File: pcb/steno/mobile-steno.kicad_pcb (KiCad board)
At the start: 2 copper layers, 188 x 92.5 mm, 65 parts, among them J1 Conn_01x02, J2 Conn_01x04, J3 Conn_01x02, K1 KEYSW, K10 KEYSW, K11 KEYSW, K12 KEYSW, K13 KEYSW, K14 KEYSW, K15 KEYSW, K16 KEYSW, K17 KEYSW, K18 KEYSW, K19 KEYSW, K2 KEYSW, K20 KEYSW, K21 KEYSW, K22 KEYSW, K23 KEYSW, K24 KEYSW, K25 KEYSW, K26 KEYSW, K27 KEYSW, K28 KEYSW, K29 KEYSW, K3 KEYSW, K30 KEYSW, K4 KEYSW, K5 KEYSW, K6 KEYSW, K7 KEYSW, K8 KEYSW, K9 KEYSW, U1 Adafruit_Feather, U2 MT25QL128ABA1ESE

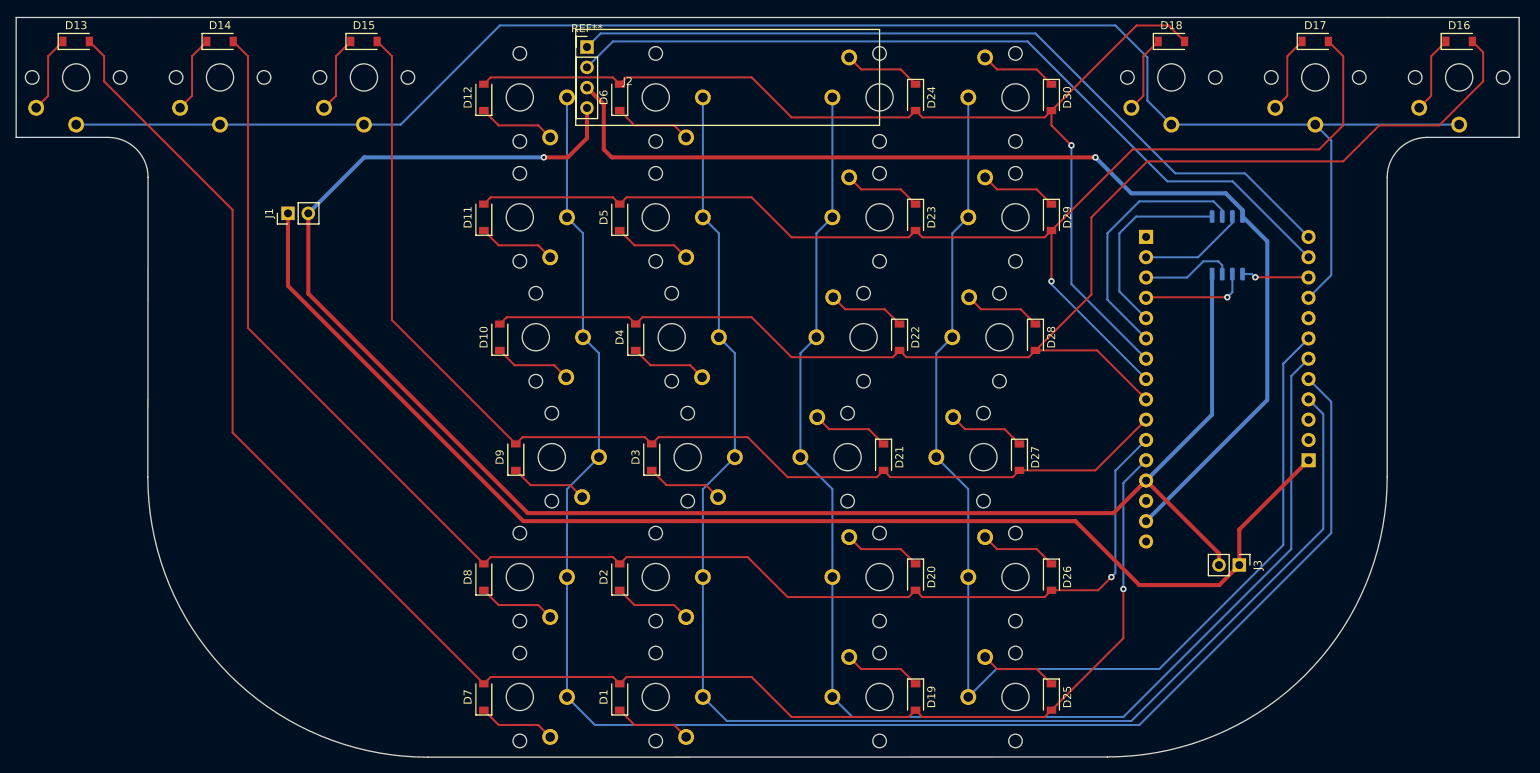
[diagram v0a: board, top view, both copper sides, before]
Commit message: Fix silkscreen and fucking flip the switches
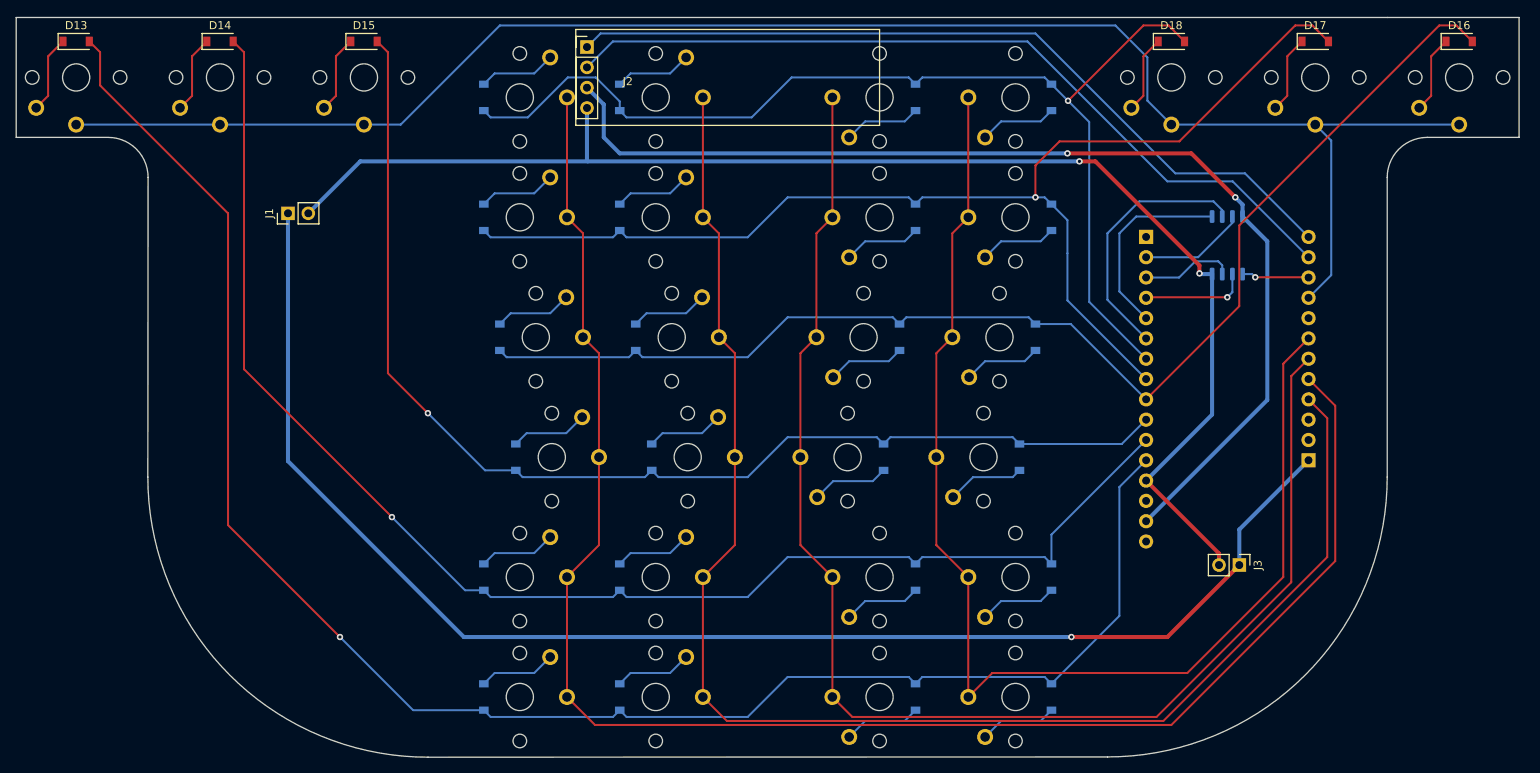
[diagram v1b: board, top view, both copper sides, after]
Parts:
- D1, D10, D11, D12, D19, D2, D20, D21, D22, D23, D24, D25, D26, D27, D28, D29, D3, D30, D4, D5, D6, D7, D8, D9, K1, K10, K11, K12, K19, K2, K20, K21, K22, K23, K24, K25, K26, K27, K28, K29, K3, K30, K4, K5, K6, K7, K8, K9: moved to B.Cu
- turned D1 to 270 degrees
- turned D10 to 270 degrees
- turned D11 to 270 degrees
- turned D12 to 270 degrees
- turned D19 to 90 degrees
- turned D2 to 270 degrees
- turned D20 to 90 degrees
- turned D21 to 90 degrees
- turned D22 to 90 degrees
- turned D23 to 90 degrees
- turned D24 to 90 degrees
- turned D25 to 90 degrees
- turned D26 to 90 degrees
- turned D27 to 90 degrees
- turned D28 to 90 degrees
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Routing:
- net GND: track 214.1 -> 172.6 mm, vias 1 -> 2
- net BAT: track 161.3 -> 179.5 mm, vias 0 -> 1
- net COL4: track 168.7 -> 155.9 mm
- net COL1: track 212.1 -> 217.3 mm
- net COL6: track 133.0 -> 137.8 mm
- net COL3: track 143.2 -> 147.4 mm, vias 0 -> 1
- net ROW2: track 205.8 -> 208.5 mm
- net ROW1: track 184.1 -> 186.8 mm
- net ROW4: track 170.2 -> 172.6 mm
- net ROW5: track 152.7 -> 155.1 mm
- net COL2: track 180.7 -> 178.6 mm
- net COL5: track 151.9 -> 150.7 mm
- net VCC: track 138.1 -> 137.6 mm, vias 1 -> 2
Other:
- board text added: "JLCJLCJLCJLC"

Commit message: Slightly improved layout and routing
- Moved thumb cluster to row 5 from 3
- Make row pins be in order
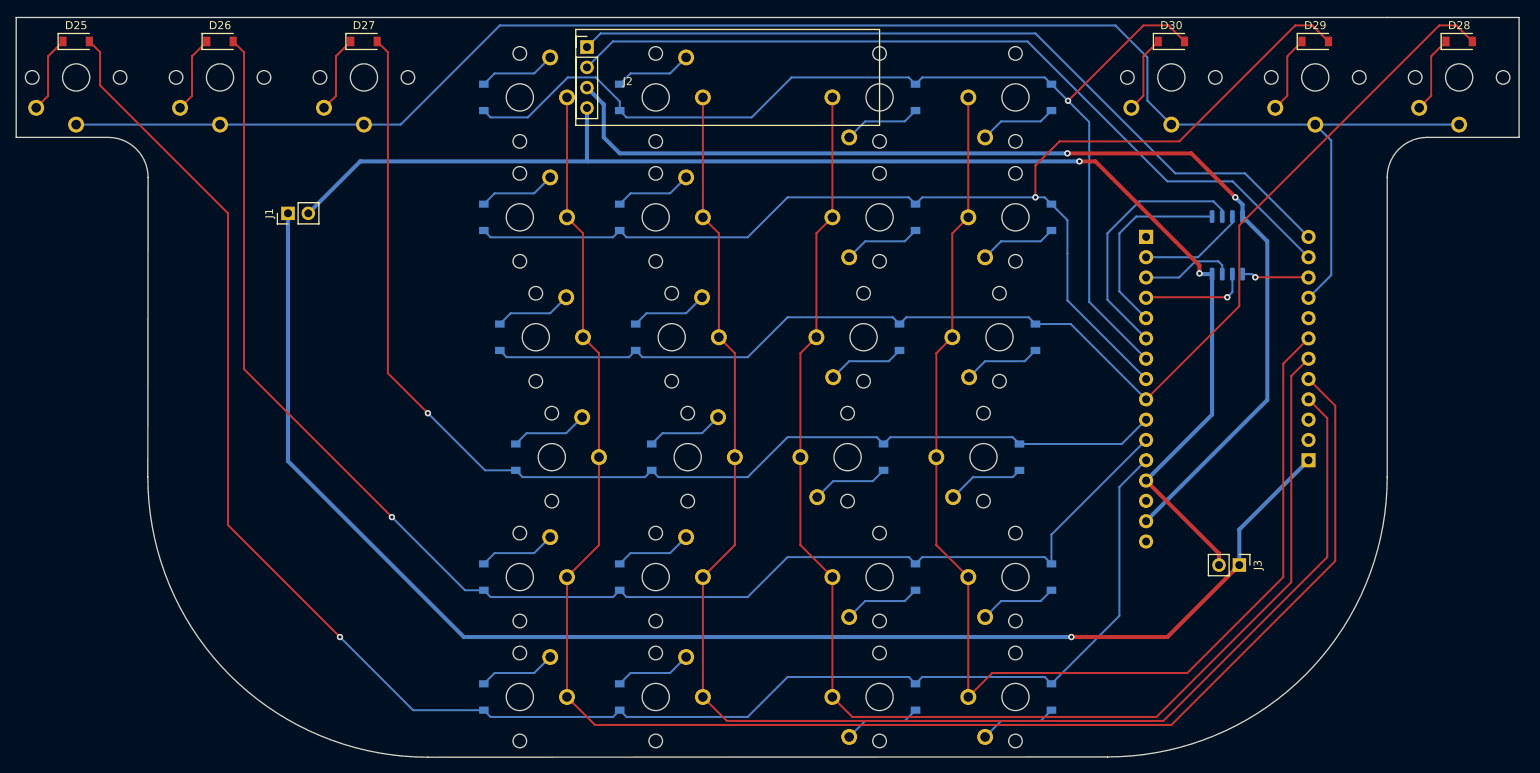
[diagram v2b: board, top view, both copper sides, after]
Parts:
- D13, D14, D15, D16, D17, D18, K13, K14, K15, K16, K17, K18: moved to B.Cu
- D25, D26, D27, D28, D29, D30, K25, K26, K27, K28, K29, K30: moved to F.Cu
- moved D25 147.0 mm to (29.4, 35.7), turned to 0 degrees
- moved K25 140.8 mm to (29.4, 40.2), turned to 0 degrees
- moved D13 133.2 mm to (134.4, 117.7), turned to 90 degrees
- moved K13 126.9 mm to (129.9, 117.7), turned to 90 degrees
- moved D26 123.7 mm to (47.4, 35.7), turned to 0 degrees
- moved K26 117.5 mm to (47.4, 40.2), turned to 0 degrees
- moved D14 109.8 mm to (134.4, 102.7), turned to 90 degrees
- moved K14 103.5 mm to (129.9, 102.7), turned to 90 degrees
- moved D27 97.1 mm to (65.4, 35.7), turned to 0 degrees
- moved K27 90.9 mm to (65.4, 40.2), turned to 0 degrees
- moved D15 83.2 mm to (130.4, 87.7), turned to 90 degrees
- moved K16 81.3 mm to (127.9, 72.7), turned to 90 degrees
- moved D16 79.2 mm to (132.4, 72.7), turned to 90 degrees
- moved K15 76.9 mm to (125.9, 87.7), turned to 90 degrees
- moved K28 66.0 mm to (202.4, 40.2), turned to 0 degrees
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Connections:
- U1 pad 22: ROW4 -> ROW3
- U1 pad 23: ROW5 -> ROW4
- U1 pad 25: ROW3 -> ROW5
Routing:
- net ROW5: track 155.1 -> 210.1 mm
- net ROW3: track 210.1 -> 172.6 mm
- net ROW4: track 172.6 -> 155.1 mm

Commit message: Update PCB
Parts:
- moved K26 12.1 mm to (59.5, 40.0), turned to 270 degrees
- moved K27 11.1 mm to (76.5, 40.0), turned to 270 degrees
- moved D1 0.61 mm to (98.0, 117.5)
- moved D10 0.61 mm to (83.0, 72.5)
- moved D11 0.61 mm to (81.0, 57.5)
- moved D12 0.61 mm to (81.0, 42.5)
- moved D2 0.61 mm to (98.0, 102.5)
- moved D27 0.61 mm to (66.0, 35.5)
- moved D3 0.61 mm to (102.0, 87.5)
- moved D4 0.61 mm to (100.0, 72.5)
- moved D5 0.61 mm to (98.0, 57.5)
- moved D6 0.61 mm to (98.0, 42.5)
- moved D7 0.61 mm to (81.0, 117.5)
- moved D8 0.61 mm to (81.0, 102.5)
- moved D9 0.61 mm to (85.0, 87.5)
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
